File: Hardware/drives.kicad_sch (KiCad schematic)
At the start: 61 parts, among them J11 DG250-3-5-02P-11-00AH, J12 DG250-3-5-02P-11-00AH, J13 DG250-3-5-02P-11-00AH, J14 DG250-3-5-02P-11-00AH, J26 DG250-3-5-02P-11-00AH, Q20 BC817-40, Q21 BC807-40, Q22 BCP53-16, Q23 BCP56-16, Q24 BC817-40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

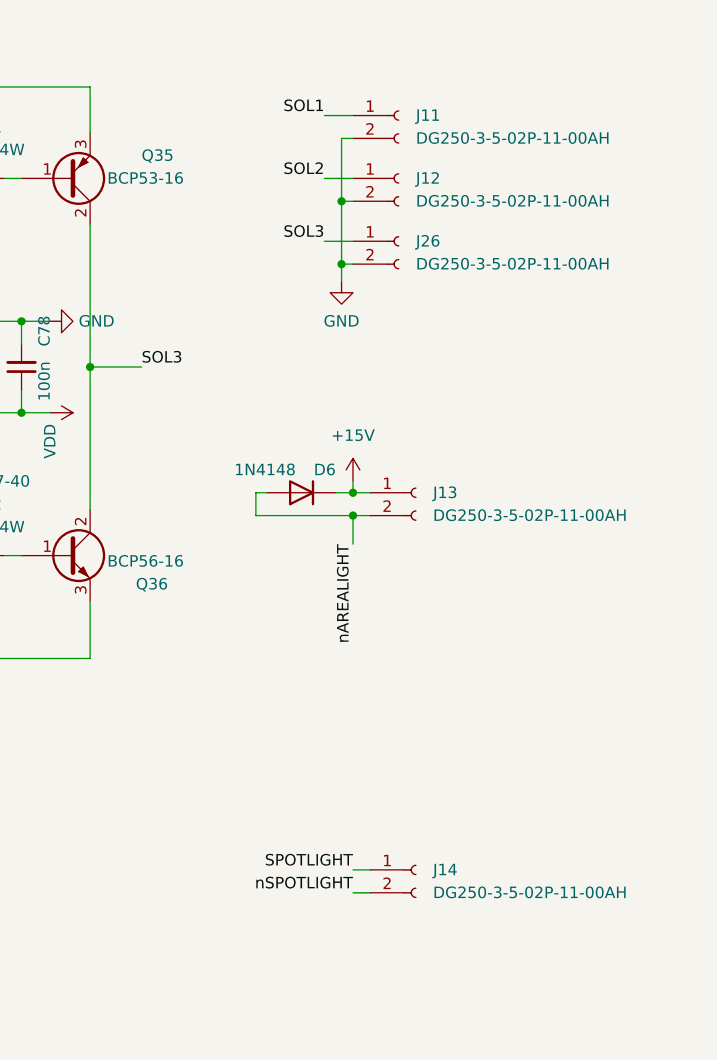
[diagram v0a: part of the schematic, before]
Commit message: Toolchain set. Timer module added. Schematic files migrated.
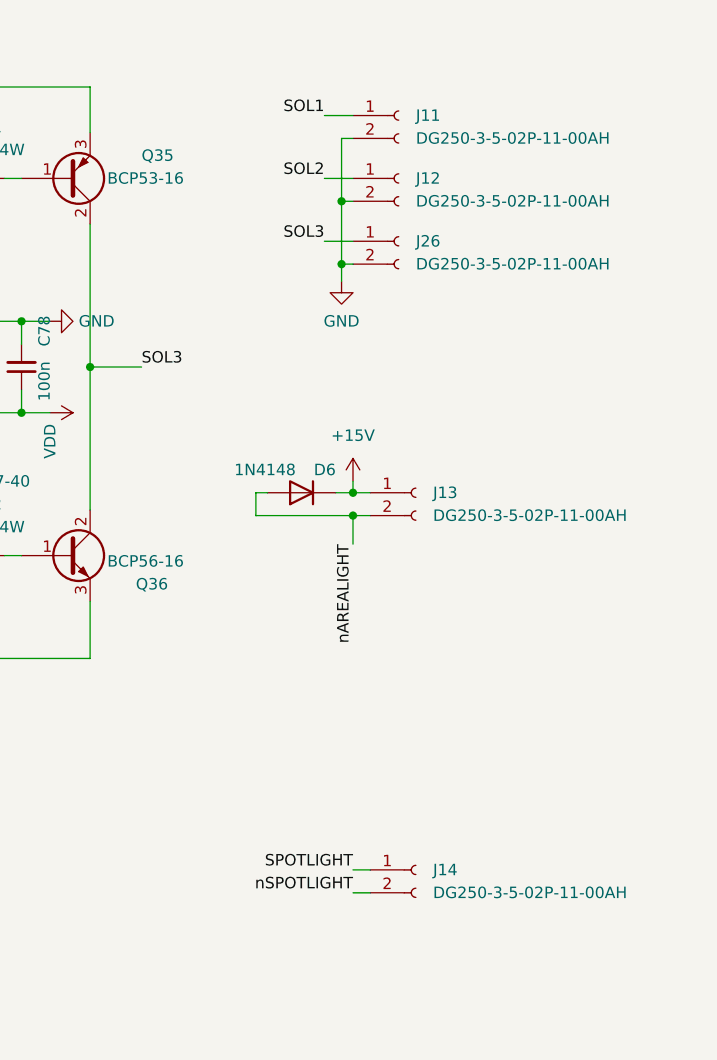
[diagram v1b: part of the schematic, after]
